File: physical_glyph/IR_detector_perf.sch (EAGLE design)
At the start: 19 parts, among them IC1 7805T, T1 BP103, U1 MCP6004-I/P, U2 LM339PWR

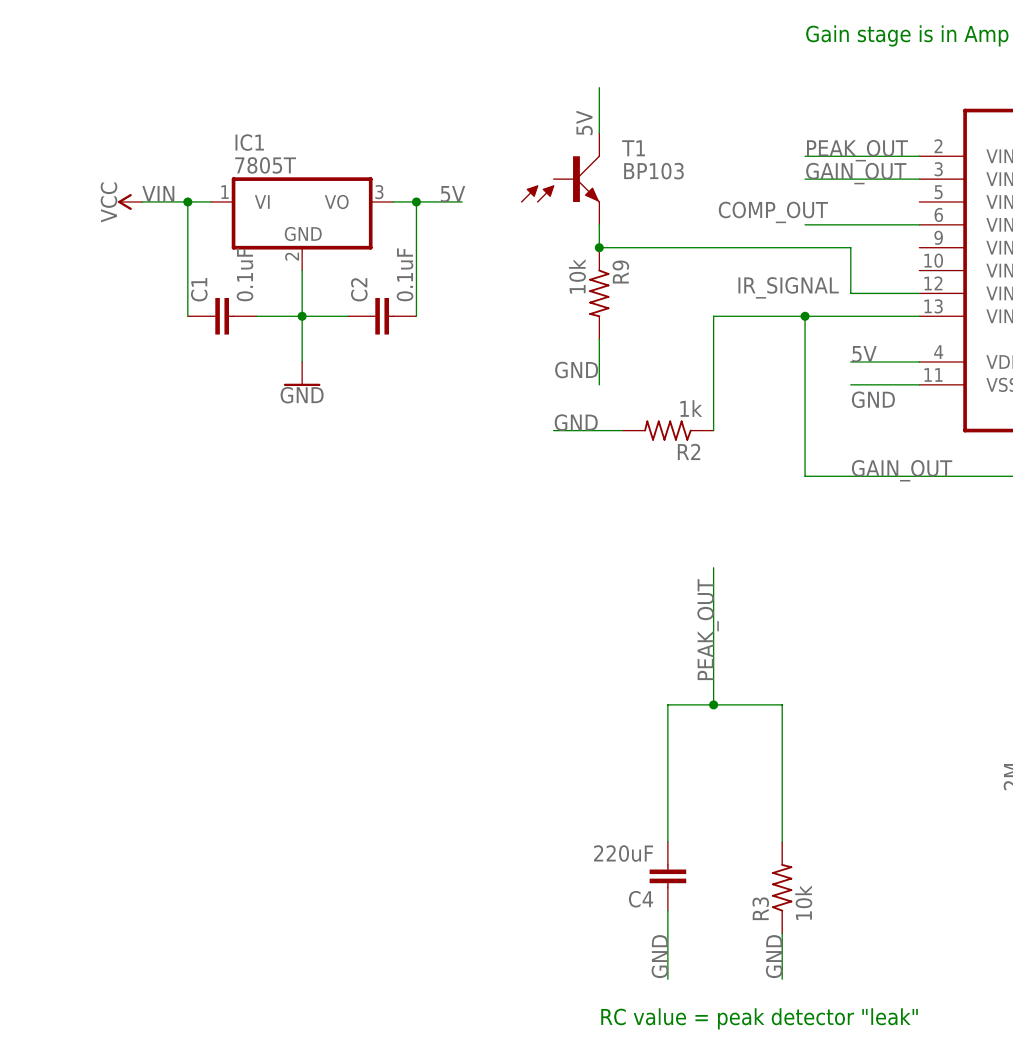
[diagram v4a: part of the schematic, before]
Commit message: Add high-pass filter
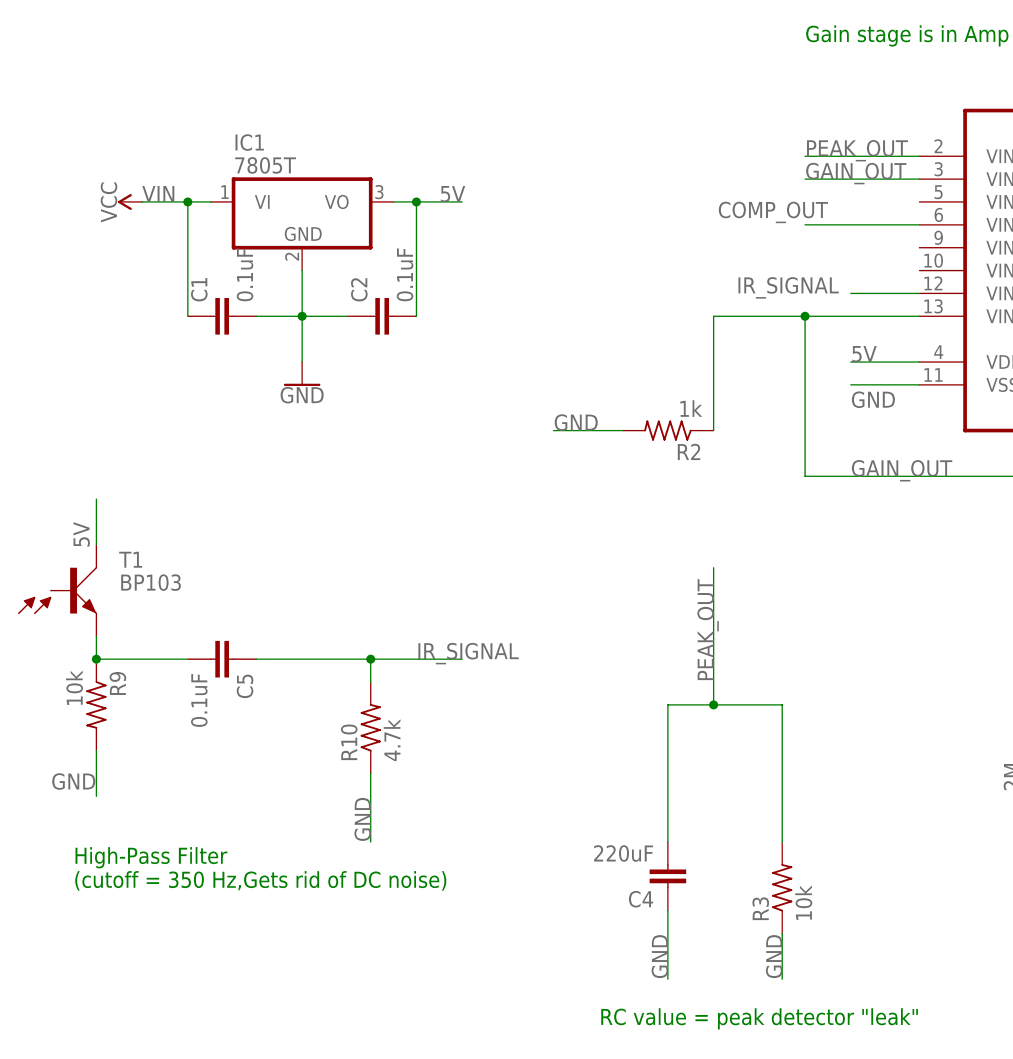
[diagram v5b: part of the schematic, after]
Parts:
- added C5: 0.1uF, resistor:C-EU025-024X044
- added R10: 4.7k, rcl:R-US_0204/2V
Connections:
- new net N$1: C5.2, R9.1, T1.E
- net GND: now also R10.1
- net IR_SIGNAL: now also C5.1, R10.2; no longer R9.1, T1.E
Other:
- note added: "High-Pass Filter (cutoff = 350 Hz,Gets rid of DC noise)"
- moved on the sheet: R9, T1
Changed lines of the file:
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@@
 <part name="R8" library="rcl" library_urn="urn:adsk.eagle:library:334" deviceset="R-US_" device="0204/2V" package3d_urn="urn:adsk.eagle:package:23495/1" value="1k"/>
 <part name="R9" library="rcl" library_urn="urn:adsk.eagle:library:334" deviceset="R-US_" device="0204/2V" package3d_urn="urn:adsk.eagle:package:23495/1" value="10k"/>
+<part name="C5" library="resistor" library_urn="urn:adsk.eagle:library:348" deviceset="C-EU" device="025-024X044" package3d_urn="urn:adsk.eagle:package:26149/1" value="0.1uF"/>
+<part name="R10" library="rcl" library_urn="urn:adsk.eagle:library:334" deviceset="R-US_" device="0204/2V" package3d_urn="urn:adsk.eagle:package:23495/1" value="4.7k"/>
 </parts>
 <sheets>
@@
 <text x="78.74" y="-15.24" size="1.778" layer="91">Inverting Schmitt Trigger</text>
 <text x="119.38" y="-17.78" size="1.778" layer="91">Microcontroller output</text>
+<text x="-40.64" y="7.62" size="1.778" layer="91">High-Pass Filter
+(cutoff = 350 Hz,Gets rid of DC noise)</text>
 </plain>
 <instances>
@@
 <instance part="C1" gate="G$1" x="-25.4" y="71.12" rot="R90"/>
 <instance part="C2" gate="G$1" x="-7.62" y="71.12" rot="R90"/>
-<instance part="T1" gate="1" x="15.24" y="86.36"/>
+<instance part="T1" gate="1" x="-40.64" y="40.64"/>
 <instance part="R1" gate="G$1" x="111.76" y="73.66" rot="R180"/>
 <instance part="R2" gate="G$1" x="25.4" y="58.42" rot="R180"/>
@@
 <instance part="R5" gate="G$1" x="139.7" y="10.16" rot="R180"/>
 <instance part="R8" gate="G$1" x="124.46" y="10.16" rot="R180"/>
-<instance part="R9" gate="G$1" x="17.78" y="73.66" rot="R270"/>
+<instance part="R9" gate="G$1" x="-38.1" y="27.94" rot="R270"/>
+<instance part="C5" gate="G$1" x="-22.86" y="33.02" rot="R270"/>
+<instance part="R10" gate="G$1" x="-7.62" y="25.4" rot="R90"/>
 </instances>
 <busses>
@@
 <segment>
 <pinref part="T1" gate="1" pin="C"/>
-<wire x1="17.78" y1="91.44" x2="17.78" y2="96.52" width="0.1524" layer="91"/>
-<label x="15.24" y="93.98" size="1.778" layer="95" rot="R270"/>
+<wire x1="-38.1" y1="45.72" x2="-38.1" y2="50.8" width="0.1524" layer="91"/>
+<label x="-40.64" y="48.26" size="1.778" layer="95" rot="R270"/>
 </segment>
 <segment>
@@
 <segment>
 <pinref part="R9" gate="G$1" pin="2"/>
-<wire x1="17.78" y1="68.58" x2="17.78" y2="63.5" width="0.1524" layer="91"/>
-<label x="17.78" y="66.04" size="1.778" layer="95" rot="R180"/>
+<wire x1="-38.1" y1="22.86" x2="-38.1" y2="17.78" width="0.1524" layer="91"/>
+<label x="-38.1" y="20.32" size="1.778" layer="95" rot="R180"/>
 </segment>
 <segment>
@@
 <label x="12.7" y="58.42" size="1.778" layer="95"/>
 </segment>
+<segment>
+<pinref part="R10" gate="G$1" pin="1"/>
+<wire x1="-7.62" y1="20.32" x2="-7.62" y2="12.7" width="0.1524" layer="91"/>
+<label x="-7.62" y="12.7" size="1.778" layer="95" rot="R90"/>
+</segment>
 </net>
 <net name="IR_SIGNAL" class="0">
 <segment>
-<pinref part="T1" gate="1" pin="E"/>
-<wire x1="17.78" y1="81.28" x2="17.78" y2="78.74" width="0.1524" layer="91"/>
 <pinref part="U1" gate="A" pin="VIND+"/>
-<wire x1="17.78" y1="78.74" x2="45.72" y2="78.74" width="0.1524" layer="91"/>
-<wire x1="45.72" y1="78.74" x2="45.72" y2="73.66" width="0.1524" layer="91"/>
 <wire x1="45.72" y1="73.66" x2="53.34" y2="73.66" width="0.1524" layer="91"/>
 <label x="33.02" y="73.66" size="1.778" layer="95"/>
-<pinref part="R9" gate="G$1" pin="1"/>
-<junction x="17.78" y="78.74"/>
+</segment>
+<segment>
+<pinref part="C5" gate="G$1" pin="1"/>
+<wire x1="-20.32" y1="33.02" x2="-7.62" y2="33.02" width="0.1524" layer="91"/>
+<pinref part="R10" gate="G$1" pin="2"/>
+<wire x1="-7.62" y1="33.02" x2="-7.62" y2="30.48" width="0.1524" layer="91"/>
+<wire x1="-7.62" y1="33.02" x2="2.54" y2="33.02" width="0.1524" layer="91"/>
+<junction x="-7.62" y="33.02"/>
+<label x="-2.54" y="33.02" size="1.778" layer="95"/>
 </segment>
 </net>
@@
 </segment>
 </net>
+<net name="N$1" class="0">
+<segment>
+<pinref part="T1" gate="1" pin="E"/>
+<wire x1="-38.1" y1="35.56" x2="-38.1" y2="33.02" width="0.1524" layer="91"/>
+<pinref part="R9" gate="G$1" pin="1"/>
+<pinref part="C5" gate="G$1" pin="2"/>
+<wire x1="-38.1" y1="33.02" x2="-27.94" y2="33.02" width="0.1524" layer="91"/>
+<junction x="-38.1" y="33.02"/>
+</segment>
+</net>

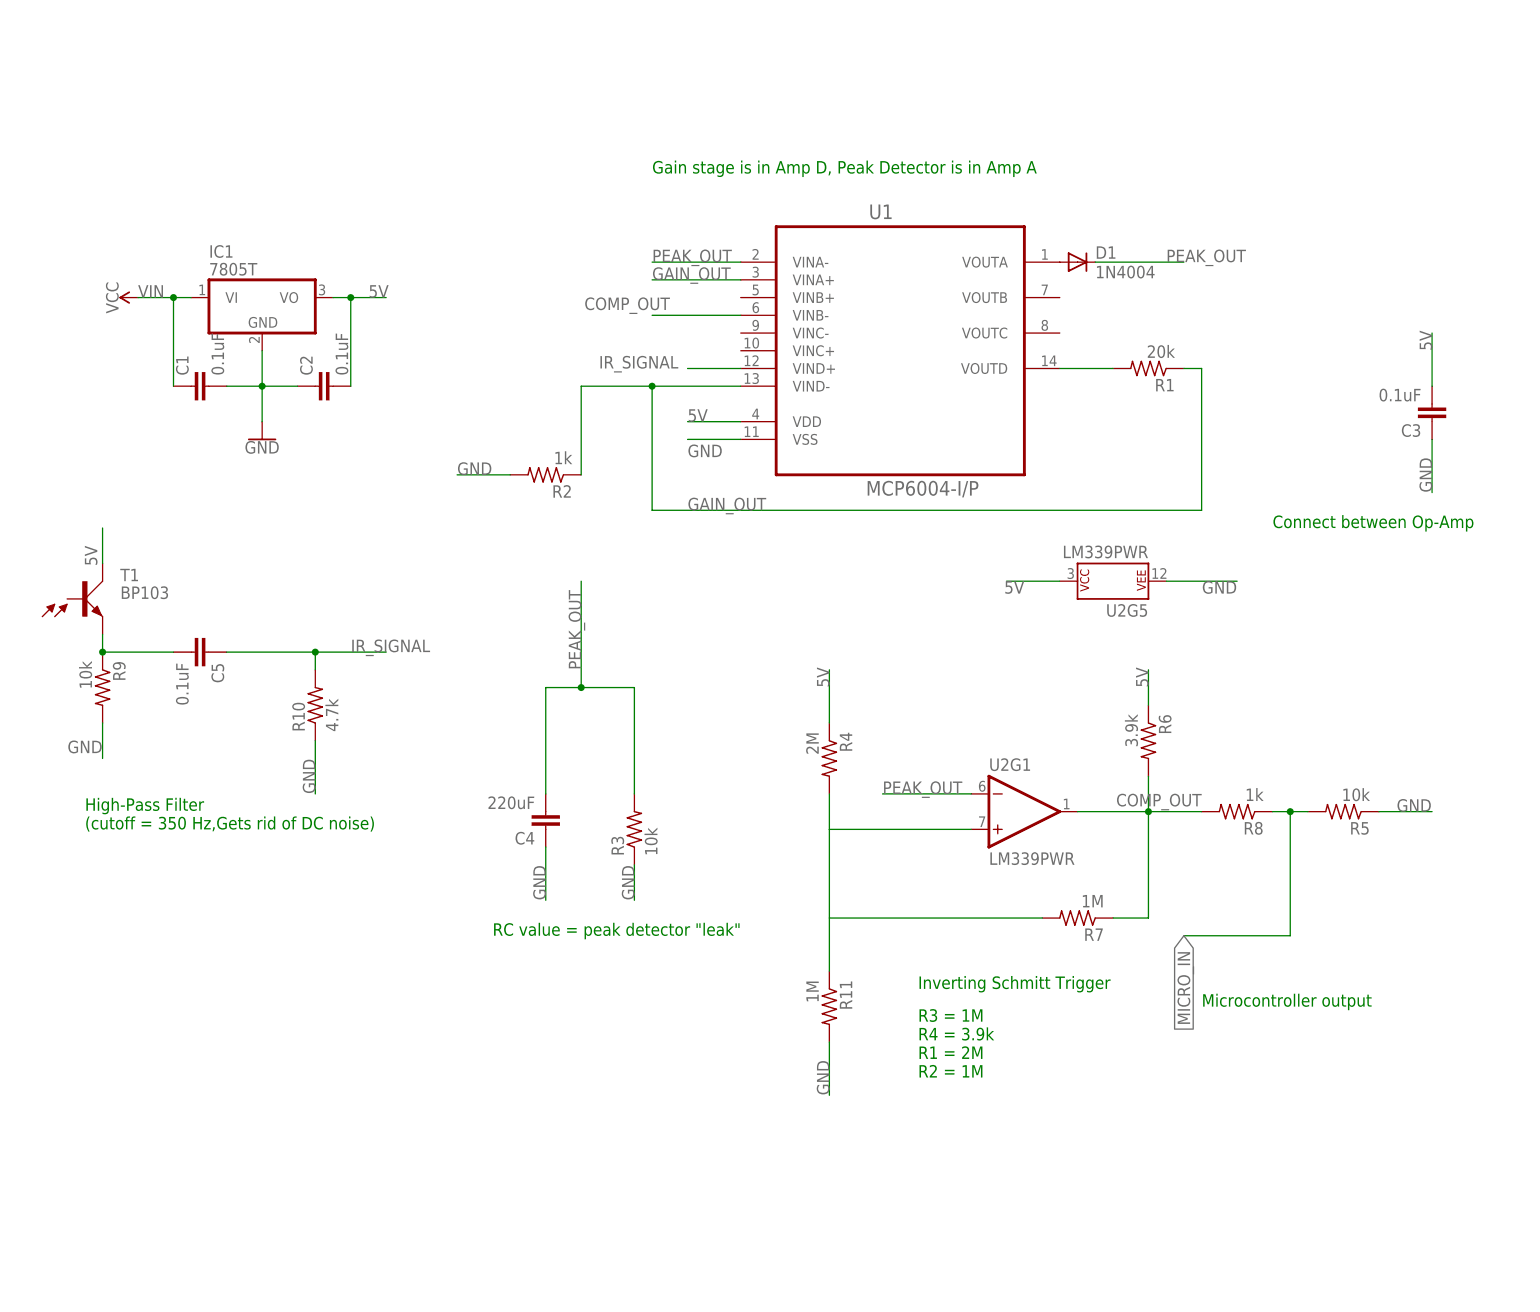
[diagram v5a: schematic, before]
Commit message: Add 2nd gain stage, split rail, and AC coupling
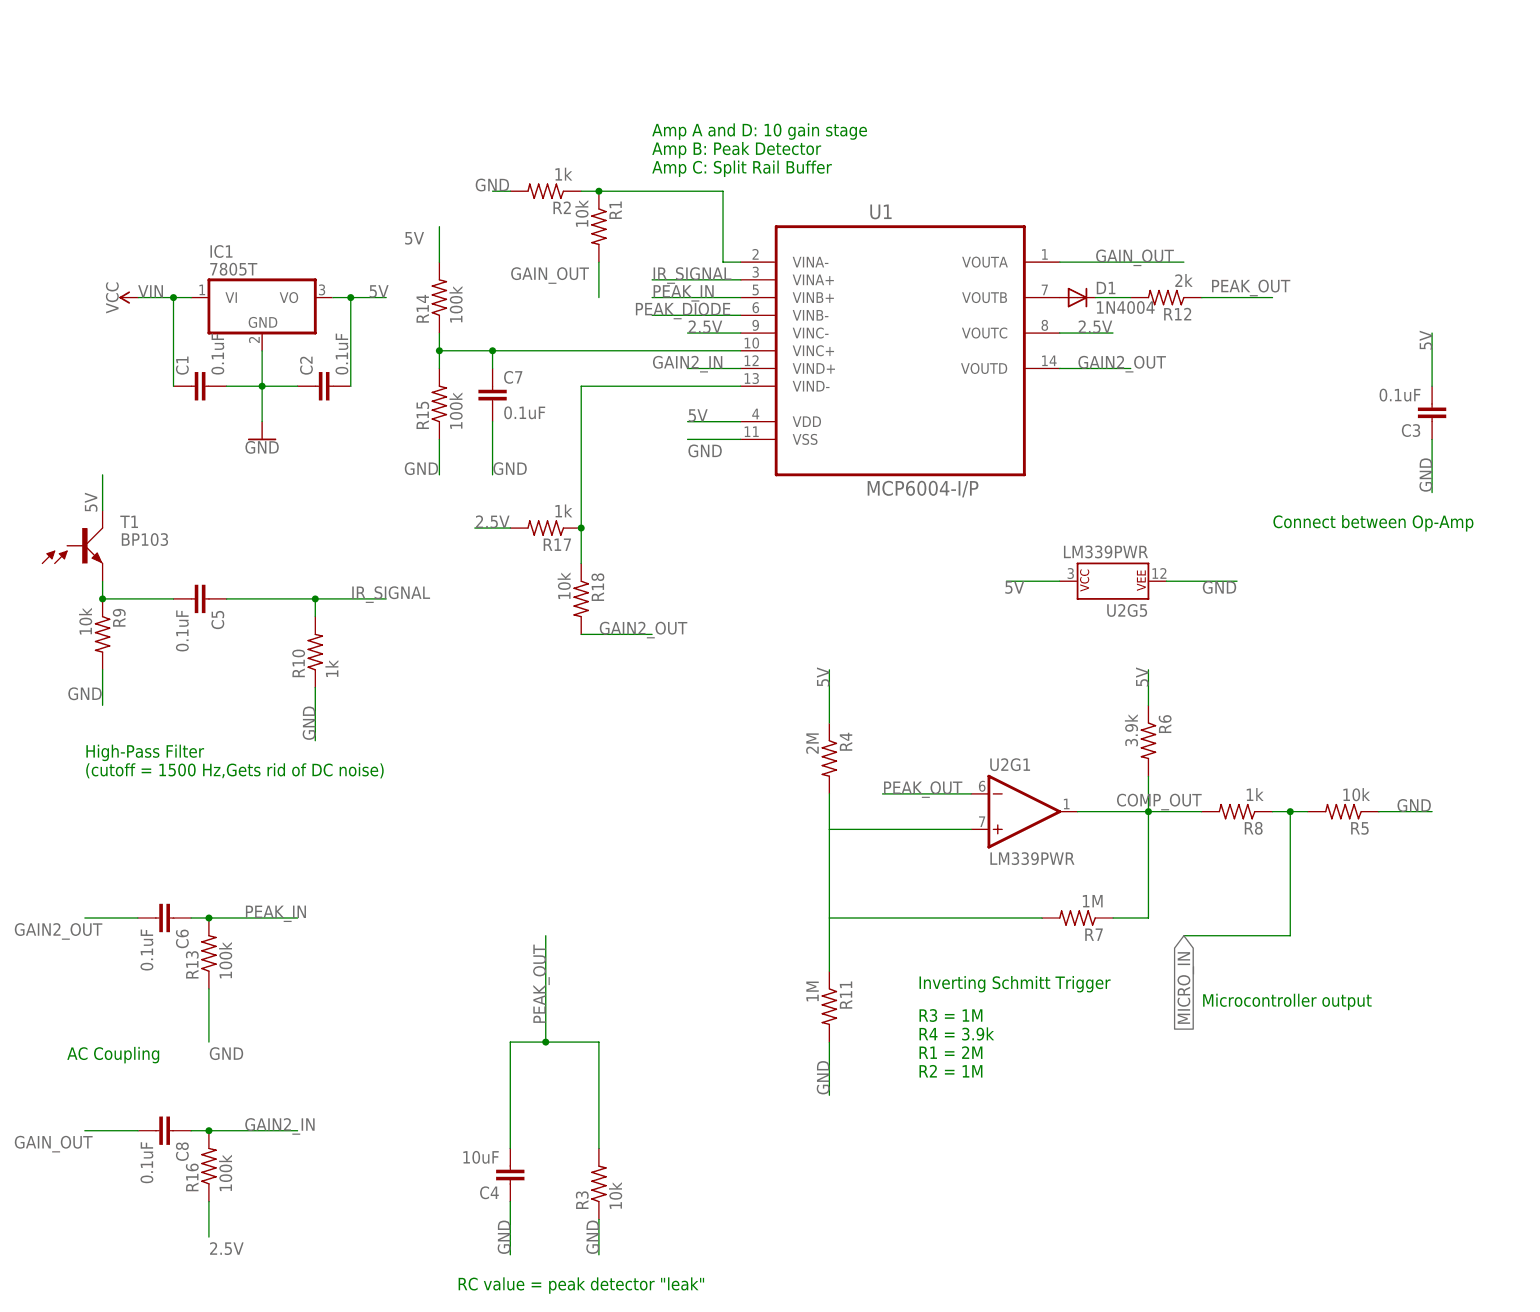
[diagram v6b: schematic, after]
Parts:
- added C6, C7, C8: 0.1uF, resistor:C-EU025-024X044
- added R12: 2k, rcl:R-US_0204/2V
- added R13, R14, R15, R16: 100k, rcl:R-US_0204/2V
- added R17: 1k, rcl:R-US_0204/2V
- added R18: 10k, rcl:R-US_0204/2V
- C4: value 220uF -> 10uF
- R1: value 20k -> 10k
- R10: value 4.7k -> 1k
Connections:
- removed net N$31: R1.2
- new net 2.5V: R16.1, R17.2, U1.VINC-, U1.VOUTC
- new net GAIN2_IN: C8.1, R16.2, U1.VIND+
- new net GAIN2_OUT: C6.2, R18.2, U1.VOUTD
- new net N$2: D1.A, U1.VOUTB
- new net N$4: C7.1, R14.1, R15.2, U1.VINC+
- new net N$5: R1.1, R2.1, U1.VINA-
- new net PEAK_DIODE: D1.C, R12.2, U1.VINB-
- new net PEAK_IN: C6.1, R13.2, U1.VINB+
- net 5V: now also R14.2
- net COMP_OUT: no longer U1.VINB-
- net GAIN_OUT: now also C8.2, R1.2, U1.VOUTA; no longer R1.1, R2.1, U1.VINA+, U1.VIND-
- net GND: now also C7.2, R13.1, R15.1
- net IR_SIGNAL: now also U1.VINA+; no longer U1.VIND+
- net N$3: now also R17.1, R18.1, U1.VIND-; no longer D1.A, U1.VOUTA
- net PEAK_OUT: now also R12.1; no longer D1.C, U1.VINA-
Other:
- note added: "AC Coupling"
- note added: "Amp A and D: 10 gain stage Amp B: Peak Detector Amp C: Split Rail Buffer"
- note added: "High-Pass Filter (cutoff = 1500 Hz,Gets rid of DC noise)"
- note removed: "Gain stage is in Amp D, Peak Detector is in Amp A"
- note removed: "High-Pass Filter (cutoff = 350 Hz,Gets rid of DC noise)"
- moved on the sheet: C4, C5, D1, R1, R10, R2, R3, R9, T1
